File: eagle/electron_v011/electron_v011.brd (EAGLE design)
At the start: 20.3 x 50.8 mm, 92 parts, among them J1 SIM-NANO-4FF, J2 IPEX-20279-001E, U1 U-BLOX-SARA-U260, U2 SN74AVC4T245, U3 STM32F205RG, U4 MAX1704X, U5 SN74LVC1G07, U6 SN74LVC1G07, U8 SN74AVC4T245, X1 USB-MICROB, Y1 32Khz, Y2 26Mhz

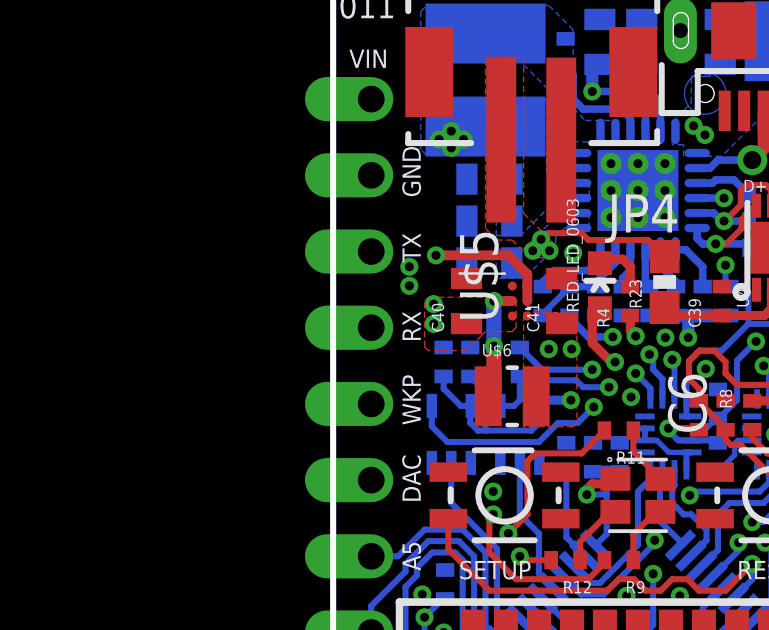
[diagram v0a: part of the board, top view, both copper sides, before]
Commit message: Replaced LM3281 with TPS62291 in schematic and updated circuit
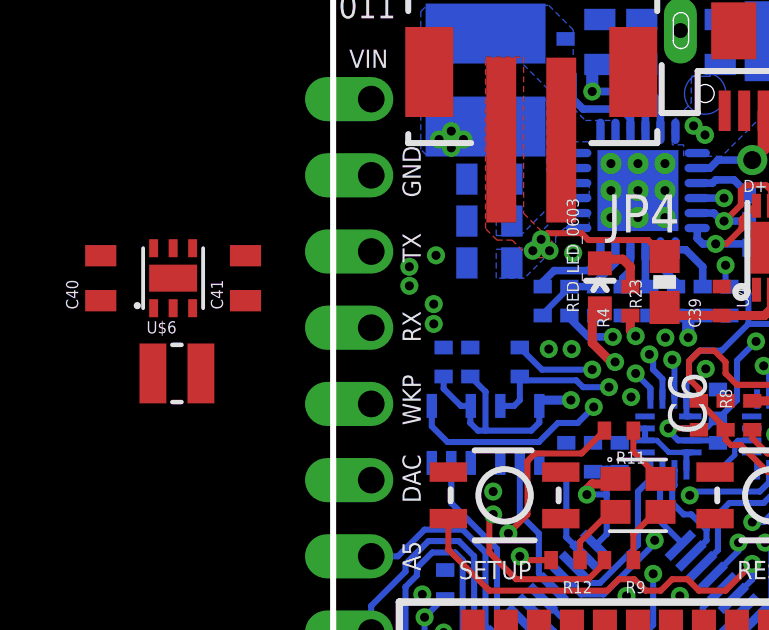
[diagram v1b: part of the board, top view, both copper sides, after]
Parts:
- C40, C41: value 2.2uF -> 10uF
- U$5: value (none) -> TPS62291DRV; device Particle:DSBGA -> Particle:S-PWSON-N6
- U$6: value 0.47uH -> 2.2uH
- moved C40 12.2 mm to (-7.75, 41.0)
- moved U$5 11.6 mm to (-5.33, 41.0), turned to 0 degrees
- moved U$6 11.2 mm to (-5.21, 37.8)
- moved C41 10.6 mm to (-2.92, 41.0)
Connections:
- net +3V3: now also U$5.P$3; no longer U$5.A1
- net +3V8: now also U$5.P$4, U$5.P$5; no longer U$5.A2, U$5.B1, U$5.C1
- net GND: now also U$5.P$2, U$5.P$6, U$5.TP; no longer U$5.C2
- net N$3: now also U$5.P$1; no longer U$5.B2
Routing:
- net +3V8: track 56.7 -> 52.5 mm
- net N$3: track 3.87 -> 0.00 mm, vias 2 -> 0
- removed copper zone on layer 1, net +3V3

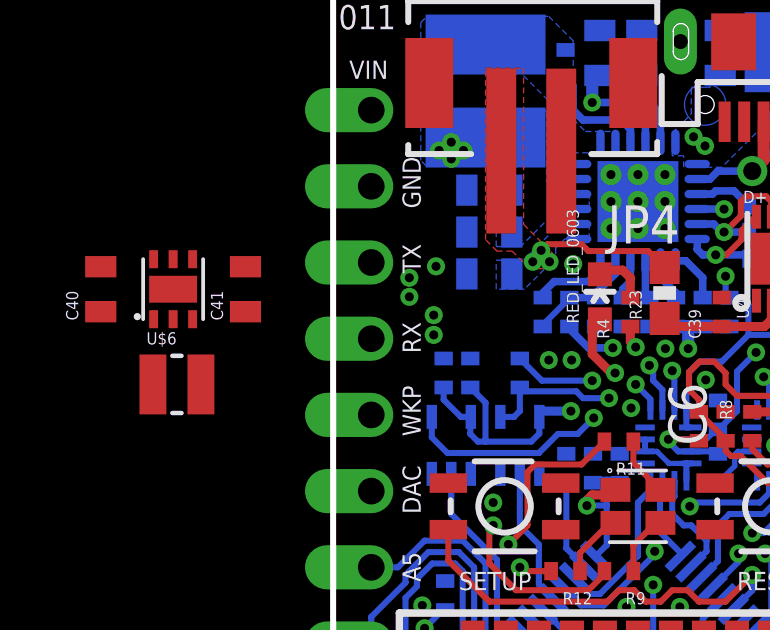
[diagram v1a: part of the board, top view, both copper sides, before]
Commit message: 2.2uH inductor reused for 3.3V circuit, components placed and locked
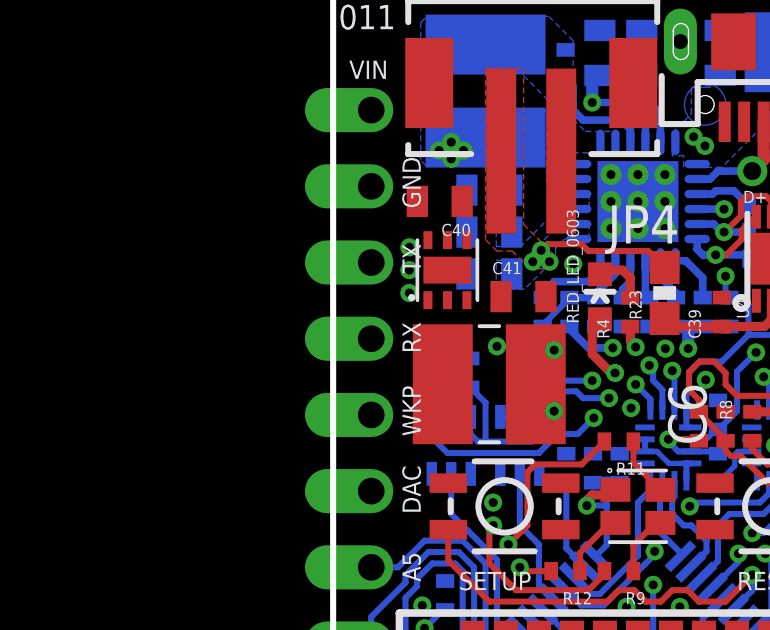
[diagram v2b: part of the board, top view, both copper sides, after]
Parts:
- U$6: device Particle:INDUCTOR-0805 -> Particle:INDUCTOR-4020
- moved C40 11.7 mm to (3.55, 43.9), turned to 180 degrees
- moved U$6 10.4 mm to (5.20, 37.9)
- moved C41 9.27 mm to (6.34, 40.8), turned to 0 degrees
- moved U$5 9.17 mm to (3.81, 41.7)
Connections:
- net +3V3: now also U$6.P$2; no longer U$6.2
- net N$3: now also U$6.P$1; no longer U$6.1
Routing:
- net +3V8: track 52.5 -> 46.4 mm, vias 12 -> 9
- net V_BCKP: track 41.8 -> 41.2 mm
- net +3V3: track 55.7 -> 55.1 mm
- net GND: vias 64 -> 65

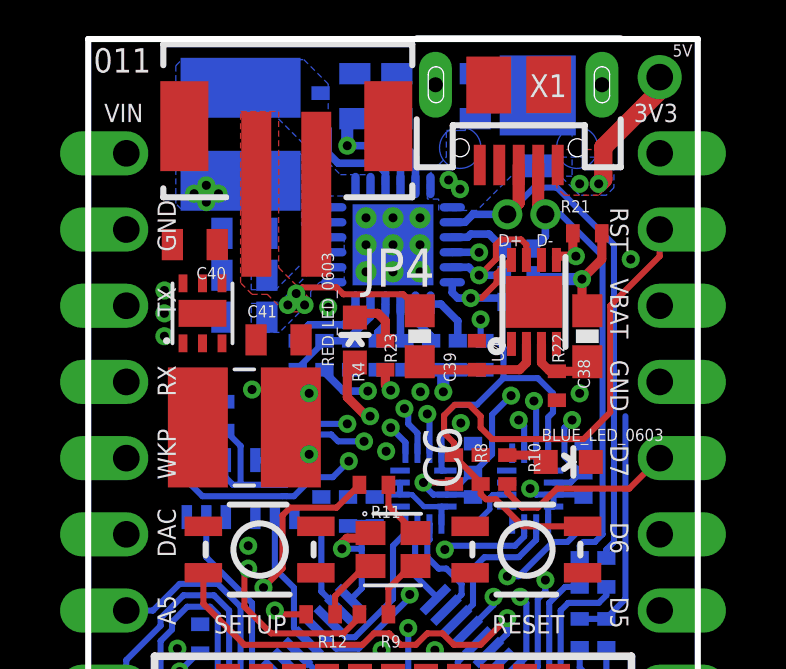
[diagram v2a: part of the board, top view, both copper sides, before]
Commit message: Completed v011 PCB routing for revised 3.3V power circuit #19
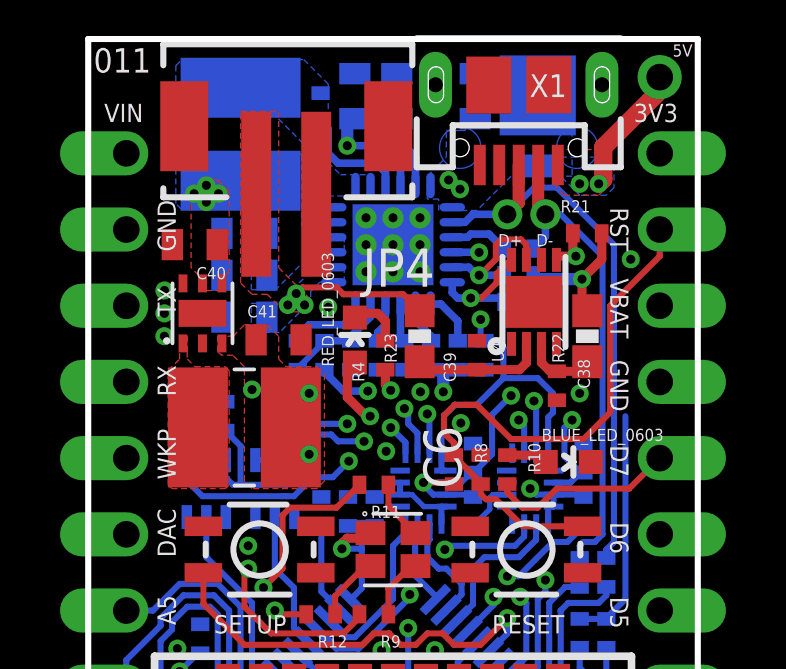
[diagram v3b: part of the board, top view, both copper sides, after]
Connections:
- net N$3 renamed SW2
- net SW renamed SW1
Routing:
- net +3V8: track 46.4 -> 54.1 mm
- added copper zone on layer 1, net +3V3
- added copper zone on layer 1, net SW2
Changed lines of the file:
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@@
 <layer number="21" name="tPlace" color="16" fill="1" visible="yes" active="yes"/>
 <layer number="22" name="bPlace" color="14" fill="1" visible="no" active="yes"/>
-<layer number="23" name="tOrigins" color="15" fill="1" visible="yes" active="yes"/>
+<layer number="23" name="tOrigins" color="15" fill="1" visible="no" active="yes"/>
 <layer number="24" name="bOrigins" color="15" fill="1" visible="no" active="yes"/>
 <layer number="25" name="tNames" color="7" fill="1" visible="no" active="yes"/>
@@
 <contactref element="U$5" pad="P$3"/>
 <contactref element="U$6" pad="P$2"/>
-<wire x1="4.46" y1="40.656" x2="5.5955" y2="40.7718" width="0" layer="19" extent="1-1"/>
-<wire x1="5.461" y1="39.116" x2="5.5955" y2="40.7718" width="0" layer="19" extent="1-1"/>
-<wire x1="6.7548" y1="37.8524" x2="6.873" y2="36.957" width="0" layer="19" extent="1-16"/>
+<polygon width="0.1524" layer="1" thermals="no" rank="2">
+<vertex x="4.318" y="40.894"/>
+<vertex x="4.826" y="40.894"/>
+<vertex x="5.207" y="41.275"/>
+<vertex x="5.969" y="41.275"/>
+<vertex x="6.35" y="40.894"/>
+<vertex x="6.35" y="40.132"/>
+<vertex x="6.604" y="39.878"/>
+<vertex x="7.62" y="39.878"/>
+<vertex x="7.874" y="39.624"/>
+<vertex x="7.874" y="36.068"/>
+<vertex x="7.62" y="35.814"/>
+<vertex x="5.461" y="35.814"/>
+<vertex x="5.207" y="36.068"/>
+<vertex x="5.207" y="39.878"/>
+<vertex x="4.826" y="40.259"/>
+<vertex x="4.445" y="40.259"/>
+<vertex x="4.318" y="40.386"/>
+</polygon>
 </signal>
 <signal name="!RST">
@@
 <wire x1="17.399" y1="41.91" x2="17.399" y2="38.354" width="0.2032" layer="1"/>
 <wire x1="17.399" y1="38.354" x2="16.51" y2="37.465" width="0.2032" layer="1"/>
-<wire x1="13.462" y1="37.465" x2="16.51" y2="37.465" width="0.2032" layer="1"/>
-<wire x1="12.7" y1="38.608" x2="13.081" y2="38.227" width="0.2032" layer="1"/>
-<wire x1="13.081" y1="38.227" x2="13.081" y2="37.846" width="0.2032" layer="1"/>
+<wire x1="14.097" y1="37.465" x2="16.51" y2="37.465" width="0.2032" layer="1"/>
 <wire x1="12.192" y1="36.8554" x2="12.2428" y2="36.8554" width="0.2032" layer="1"/>
 <wire x1="12.2428" y1="36.8554" x2="13.081" y2="36.0172" width="0.2032" layer="1"/>
@@
 <wire x1="11.8618" y1="37.6682" x2="12.192" y2="37.338" width="0.2032" layer="1"/>
 <wire x1="12.192" y1="37.338" x2="12.192" y2="36.9316" width="0.2032" layer="1"/>
-<wire x1="12.2174" y1="38.608" x2="12.7" y2="38.608" width="0.2032" layer="1"/>
-<wire x1="13.081" y1="37.846" x2="13.462" y2="37.465" width="0.2032" layer="1"/>
+<wire x1="12.2174" y1="38.608" x2="12.573" y2="38.608" width="0.2032" layer="1"/>
+<wire x1="12.573" y1="38.608" x2="12.7" y2="38.608" width="0.2032" layer="1"/>
 <wire x1="17.399" y1="41.91" x2="19.05" y2="43.561" width="0.2032" layer="1"/>
 <contactref element="JP2" pad="17"/>
@@
 <wire x1="17.399" y1="41.91" x2="19.05" y2="43.561" width="0.2032" layer="2"/>
 <wire x1="19.05" y1="43.561" x2="19.05" y2="44.45" width="0.2032" layer="2"/>
+<wire x1="14.097" y1="37.465" x2="12.954" y2="38.608" width="0.2032" layer="1"/>
+<wire x1="12.954" y1="38.608" x2="12.7" y2="38.608" width="0.2032" layer="1"/>
 </signal>
 <signal name="USB_DP">
@@
 <vertex x="2.794" y="3.937"/>
 </polygon>
-<wire x1="9.271" y1="38.227" x2="8.636" y2="38.862" width="0.3048" layer="15"/>
-<wire x1="8.636" y1="38.862" x2="8.636" y2="39.243" width="0.3048" layer="15"/>
 <wire x1="9.398" y1="38.227" x2="9.271" y2="38.227" width="0.3048" layer="15"/>
 <wire x1="8.89" y1="40.017" x2="8.636" y2="39.763" width="0.3048" layer="1"/>
@@
 <vertex x="2.413" y="4.445"/>
 </polygon>
-<wire x1="8.636" y1="39.243" x2="8.382" y2="39.497" width="0.3048" layer="15"/>
 <via x="3.5306" y="45.6438" extent="1-16" drill="0.3"/>
 <via x="4.3434" y="45.6438" extent="1-16" drill="0.3"/>
@@
 <contactref element="U$5" pad="P$4"/>
 <contactref element="U$5" pad="P$5"/>
-<wire x1="4.46" y1="42.656" x2="4.3029" y2="43.9482" width="0" layer="19" extent="1-1"/>
-<wire x1="3.81" y1="42.656" x2="4.46" y2="42.656" width="0" layer="19" extent="1-1"/>
-<wire x1="3.937" y1="45.3644" x2="4.3029" y2="43.9482" width="0" layer="19" extent="1-1"/>
-<wire x1="8.89" y1="40.017" x2="8.185" y2="43.692" width="0" layer="19" extent="1-16"/>
+<polygon width="0.1524" layer="1" thermals="no">
+<vertex x="4.445" y="42.418"/>
+<vertex x="3.683" y="42.418"/>
+<vertex x="3.683" y="42.926"/>
+<vertex x="3.429" y="43.18"/>
+<vertex x="3.429" y="45.72"/>
+<vertex x="3.81" y="46.101"/>
+<vertex x="4.318" y="46.101"/>
+<vertex x="4.699" y="45.72"/>
+<vertex x="4.699" y="43.053"/>
+<vertex x="4.572" y="42.926"/>
+<vertex x="4.572" y="42.418"/>
+</polygon>
+<wire x1="9.271" y1="38.227" x2="3.937" y2="43.561" width="0.3048" layer="15"/>
+<wire x1="3.937" y1="43.561" x2="3.937" y2="45.3644" width="0.3048" layer="15"/>
 </signal>
 <signal name="SIM_VCC">
@@
 <wire x1="15.24" y1="34.417" x2="15.24" y2="32.766" width="0.2032" layer="15"/>
 </signal>
-<signal name="SW">
+<signal name="SW1">
 <contactref element="U$1" pad="19"/>
 <contactref element="U$1" pad="20"/>
@@
 <wire x1="14.609" y1="40.637" x2="14.609" y2="40.009" width="0.3048" layer="1"/>
 </signal>
-<signal name="N$3">
+<signal name="SW2">
 <contactref element="U$5" pad="P$1"/>
 <contactref element="U$6" pad="P$1"/>
-<wire x1="3.6548" y1="37.8524" x2="3.16" y2="40.656" width="0" layer="19" extent="1-1"/>
+<polygon width="0.1524" layer="1" thermals="no" rank="3">
+<vertex x="3.048" y="40.894"/>
+<vertex x="3.302" y="40.894"/>
+<vertex x="3.302" y="40.386"/>
+<vertex x="3.302" y="40.132"/>
+<vertex x="3.556" y="39.878"/>
+<vertex x="4.572" y="39.878"/>
+<vertex x="4.699" y="39.751"/>
+<vertex x="4.699" y="35.941"/>
+<vertex x="4.572" y="35.814"/>
+<vertex x="2.794" y="35.814"/>
+<vertex x="2.667" y="35.941"/>
+<vertex x="2.667" y="39.751"/>
+<vertex x="3.048" y="40.132"/>
+</polygon>
 </signal>
 <signal name="N$2">
